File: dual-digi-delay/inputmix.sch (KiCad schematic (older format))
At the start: 12 parts, among them U2 TL072

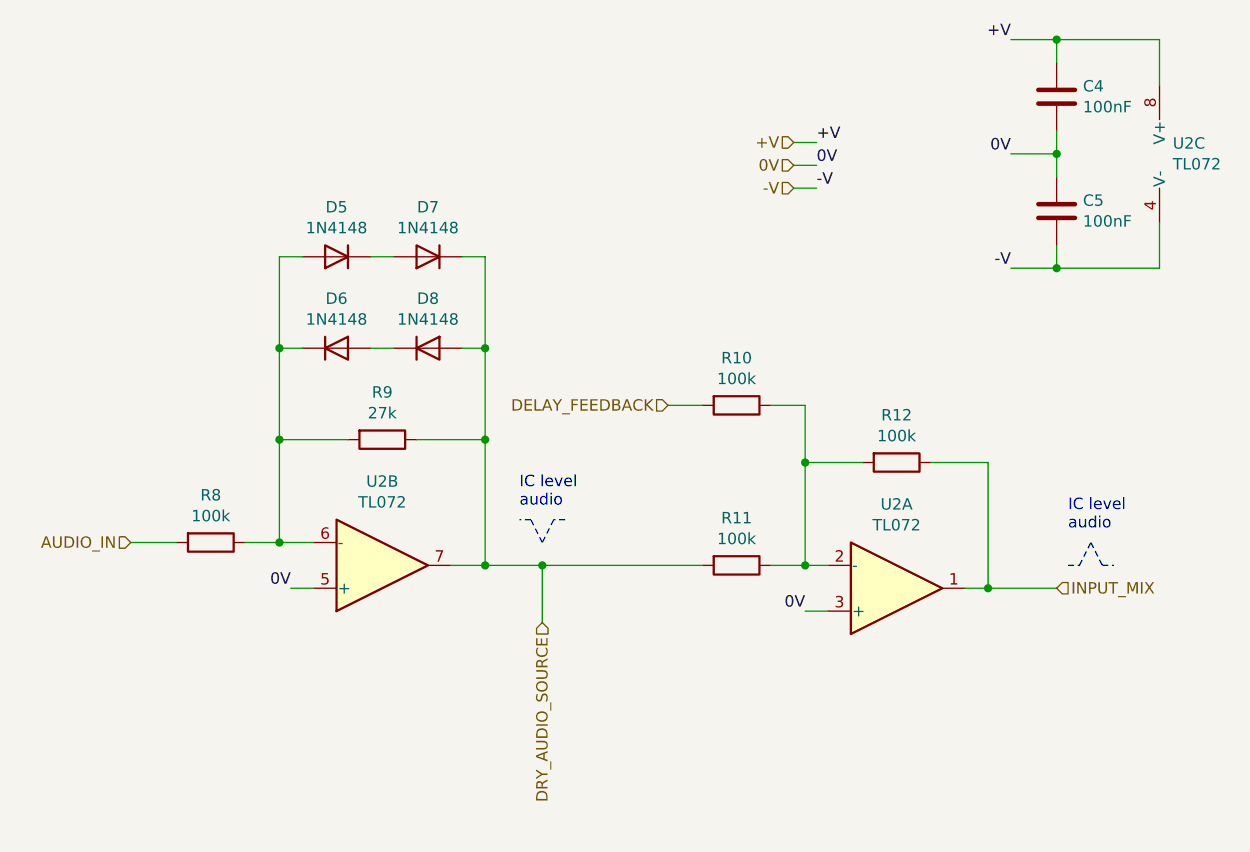
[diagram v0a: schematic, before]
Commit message: Updating digi delay to rev 2
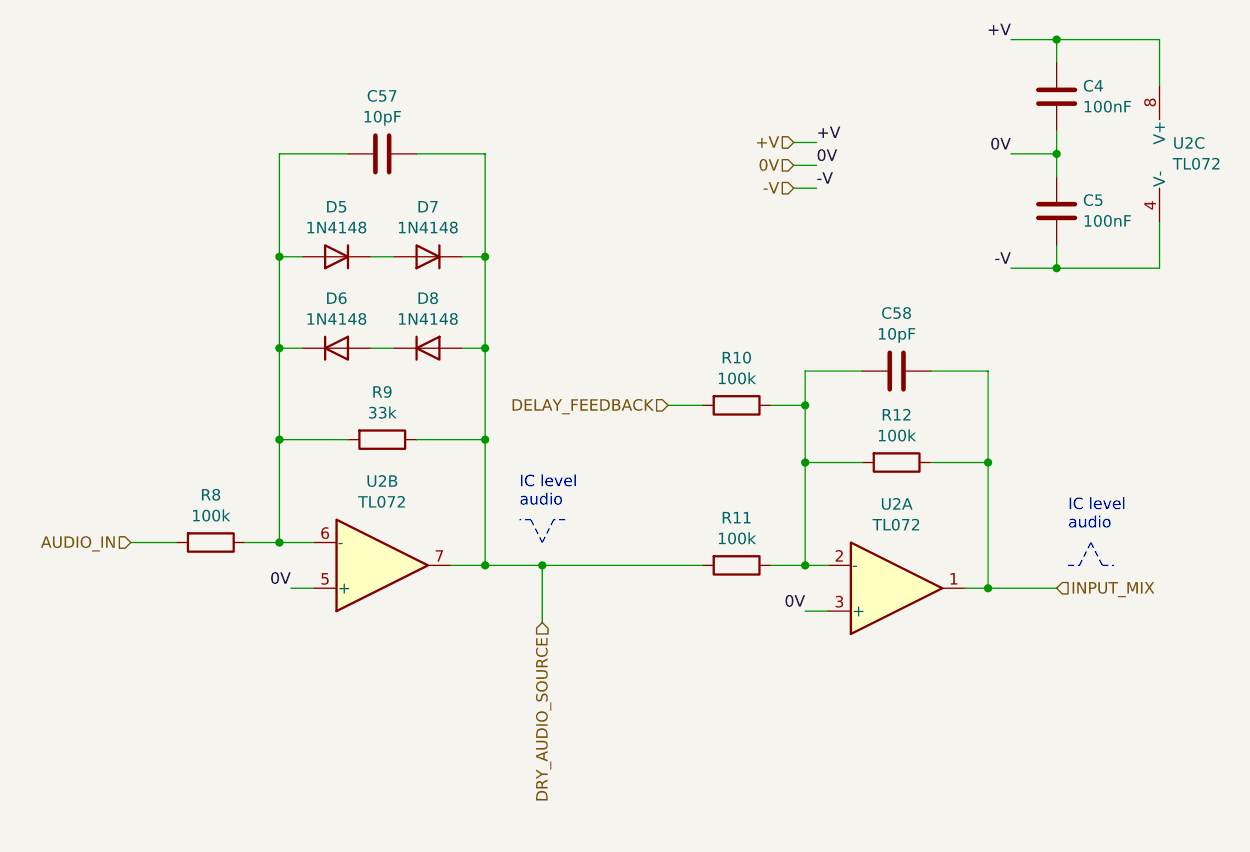
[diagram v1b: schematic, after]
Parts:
- added C57, C58: 10pF, rumblesan-footprints:C_Rect_L7.0mm_W3.5mm_P5.00mm, symbol Device:C
- R9: value 27k -> 33k
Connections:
- net DRY_AUDIO_SOURCE: now also C57.1
- net INPUT_MIX: now also C58.1
- net at R10.1, R11.1, R12.2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: now also C58.2
- net at D5.2 (A), D6.1 (K), R8.1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: now also C57.2
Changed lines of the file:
@@
 $Descr A4 11693 8268
 encoding utf-8
-Sheet 6 10
+Sheet 5 11
 Title ""
 Date ""
@@
 AR Path="/62BDC96F/62BF2200" Ref="R9"  Part="1"
 F 0 "R9" V 2993 3300 50  0000 C CNN
-F 1 "27k" V 3084 3300 50  0000 C CNN
+F 1 "33k" V 3084 3300 50  0000 C CNN
 F 2 "rumblesan-footprints:Resistor_THT_L6.3mm_D2.5mm_P10.16mm_Horizontal" V 3130 3300 50  0001 C CNN
 F 3 "~" H 3200 3300 50  0001 C CNN
@@
 Wire Wire Line
 	6600 2350 6600 2550
+$Comp
+L Device:C C57
+U 1 1 61AD415C
+P 3200 2050
+F 0 "C57" V 2948 2050 50  0000 C CNN
+F 1 "10pF" V 3039 2050 50  0000 C CNN
+F 2 "rumblesan-footprints:C_Rect_L7.0mm_W3.5mm_P5.00mm" H 3238 1900 50  0001 C CNN
+F 3 "~" H 3200 2050 50  0001 C CNN
+	1    3200 2050
+	0    1    1    0
+$EndComp
+Wire Wire Line
+	3350 2050 3650 2050
+Wire Wire Line
+	3650 2050 3650 2500
+Connection ~ 3650 2500
+Wire Wire Line
+	3050 2050 2750 2050
+Wire Wire Line
+	2750 2050 2750 2500
+Connection ~ 2750 2500
+$Comp
+L Device:C C58
+U 1 1 61ADB1FE
+P 5450 3000
+F 0 "C58" V 5198 3000 50  0000 C CNN
+F 1 "10pF" V 5289 3000 50  0000 C CNN
+F 2 "rumblesan-footprints:C_Rect_L7.0mm_W3.5mm_P5.00mm" H 5488 2850 50  0001 C CNN
+F 3 "~" H 5450 3000 50  0001 C CNN
+	1    5450 3000
+	0    1    1    0
+$EndComp
+Wire Wire Line
+	5050 3150 5050 3000
+Wire Wire Line
+	5050 3000 5300 3000
+Connection ~ 5050 3150
+Wire Wire Line
+	5600 3000 5850 3000
+Wire Wire Line
+	5850 3000 5850 3400
+Connection ~ 5850 3400
 $EndSCHEMATC
